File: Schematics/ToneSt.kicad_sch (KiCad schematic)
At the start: 18 parts

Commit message: Cosmetic upd
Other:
- moved on the sheet: Bass1, C51, C52, C53, C54, C55, C56, JP0, JP50, JP51, JP53, Middle1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

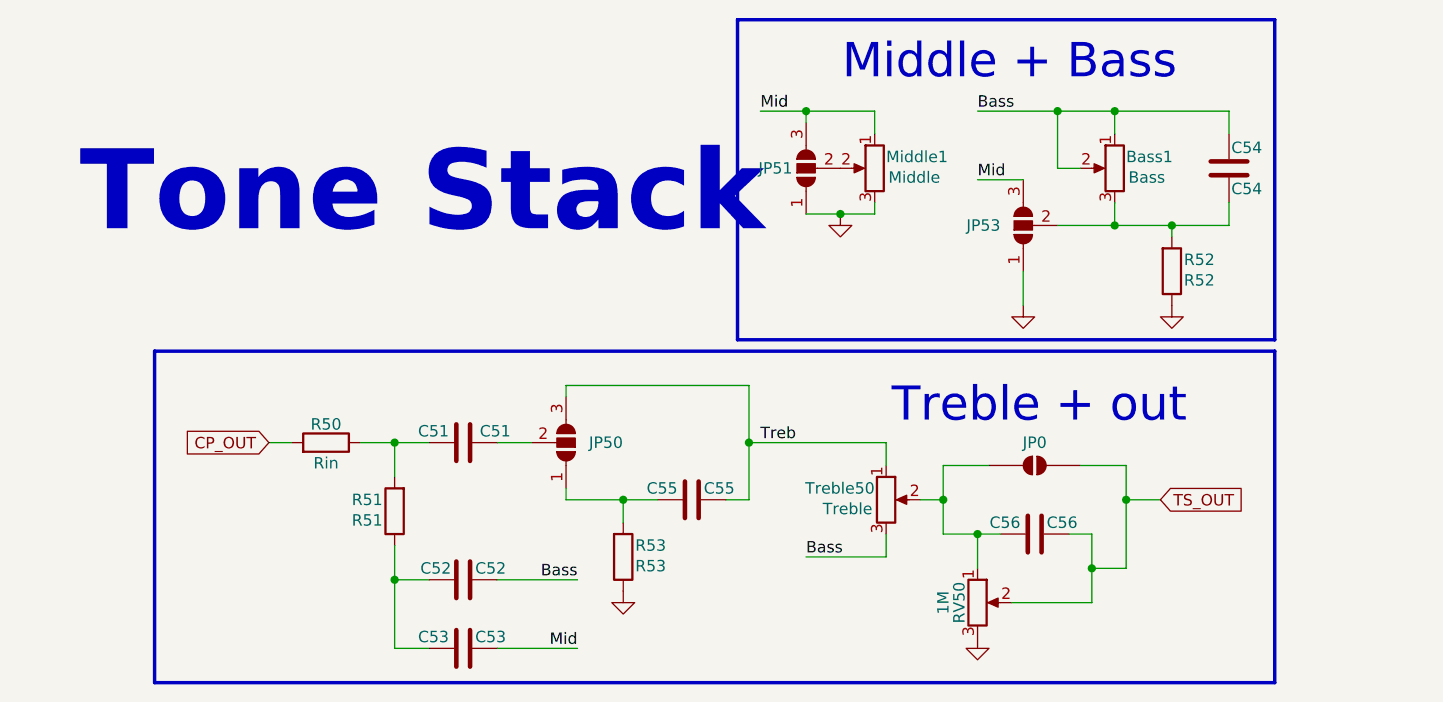
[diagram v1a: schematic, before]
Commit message: Schem. & Readme upd
volume control upd, optimized tone stack jumpers, small redactions in Readme
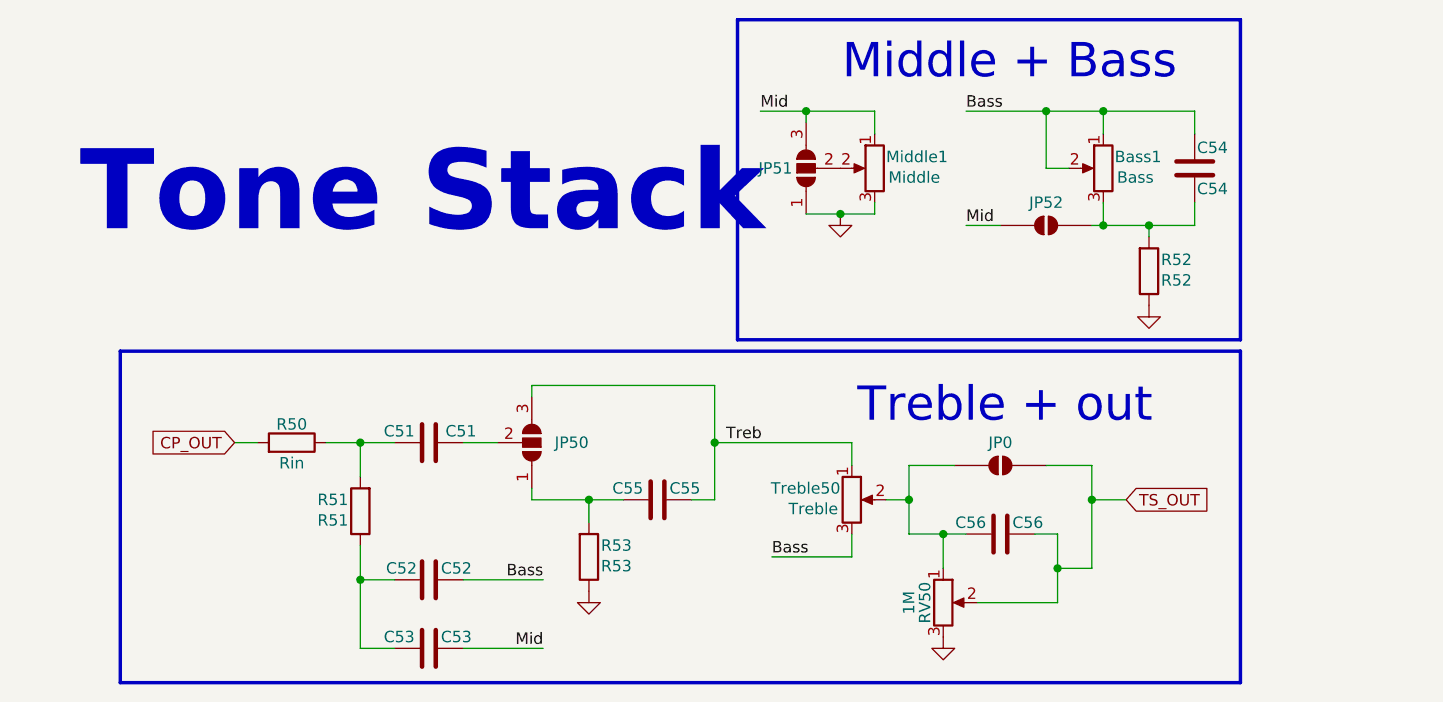
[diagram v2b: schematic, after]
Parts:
- removed JP53: SolderJumper_3_Open, Jumper:SolderJumper-3_P2.0mm_Open_TrianglePad1.0x1.5mm_NumberLabels, symbol Jumper:SolderJumper_3_Open
- added JP52: SolderJumper_2_Open, Jumper:SolderJumper-2_P1.3mm_Open_TrianglePad1.0x1.5mm, symbol Jumper:SolderJumper_2_Open
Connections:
- net Mid: now also JP52.1 (A)
- net at Bass1.3, C54.1, R52.2: now also JP52.2 (B)
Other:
- moved on the sheet: Bass1, C51, C52, C53, C54, C55, C56, JP0, JP50, R50, R51, R52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

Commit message: Version 0.1.0 Pre-Release
Reworked PCB, reanotated some components, changed some footprints
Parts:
- renumbered Treble50 to Treble1
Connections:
- net CP_OUT renamed BP_OUT
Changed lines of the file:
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@@
 		)
 	)
-	(global_label "CP_OUT"
+	(global_label "BP_OUT"
 		(shape input)
 		(at 26.67 60.96 180)
@@
 		)
 		(property "Intersheetrefs" "${INTERSHEET_REFS}"
-			(at 16.5486 60.96 0)
+			(at 16.799 60.96 0)
 			(hide yes)
 			(show_name no)
@@
 		(in_pos_files yes)
 		(dnp no)
-		(property "Reference" "Treble50"
+		(property "Reference" "Treble1"
 			(at 93.98 66.04 0)
 			(show_name no)
@@
 			(project "AMP-MA"
 				(path "/4094031b-a9da-4ac5-aaa1-42b342c92a3e/f803cc2a-45bd-4029-aa56-0c7cd35c7800"
-					(reference "Treble50")
+					(reference "Treble1")
 					(unit 1)
 				)

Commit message: Version 0.1.0 Release
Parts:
- renumbered JP0 to JP54
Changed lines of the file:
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@@
 		(in_pos_files yes)
 		(dnp no)
-		(property "Reference" "JP0"
+		(property "Reference" "JP54"
 			(at 111.76 60.96 0)
 			(show_name no)
@@
 			(project "AMP-MA"
 				(path "/4094031b-a9da-4ac5-aaa1-42b342c92a3e/f803cc2a-45bd-4029-aa56-0c7cd35c7800"
-					(reference "JP0")
+					(reference "JP54")
 					(unit 1)
 				)

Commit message: feat: start version 0.2.0 development
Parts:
- removed JP54: SolderJumper_2_Open, Jumper:SolderJumper-2_P1.3mm_Open_TrianglePad1.0x1.5mm, symbol Jumper:SolderJumper_2_Open
- added R54: 1R, Resistor_THT:R_Axial_DIN0207_L6.3mm_D2.5mm_P10.16mm_Horizontal, symbol Device:R
- C54, C55, C56, R52, R53, RV50: now not fitted
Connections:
- net GND: now also RV50.1; no longer RV50.3
- net TS_OUT: now also R54.1
- net at C56.1, Treble1.2: now also RV50.3, R54.2; no longer RV50.1
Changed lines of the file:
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@@
+	(wire
+		(pts
+			(xy 115.57 63.5) (xy 121.92 63.5)
+		)
+		(stroke
+			(width 0)
+			(type default)
+		)
+	)
 	(wire
 		(pts
@@
 	(wire
 		(pts
-			(xy 116.84 63.5) (xy 121.92 63.5)
-		)
-		(stroke
-			(width 0)
-			(type default)
-		)
-	)
-	(wire
-		(pts
 			(xy 123.19 36.83) (xy 133.35 36.83)
 		)
@@
 	(wire
 		(pts
-			(xy 101.6 63.5) (xy 106.68 63.5)
+			(xy 101.6 63.5) (xy 107.95 63.5)
 		)
 		(stroke
@@
 	)
 	(symbol
-		(lib_id "Jumper:SolderJumper_2_Open")
-		(at 111.76 63.5 0)
-		(unit 1)
-		(body_style 1)
-		(exclude_from_sim no)
-		(in_bom no)
-		(on_board yes)
-		(in_pos_files yes)
-		(dnp no)
-		(property "Reference" "JP54"
-			(at 111.76 60.96 0)
-			(show_name no)
-			(do_not_autoplace yes)
-			(effects
-				(font
-					(size 1.27 1.27)
-				)
-			)
-		)
-		(property "Value" "SolderJumper_2_Open"
-			(at 111.76 59.69 0)
-			(hide yes)
-			(show_name no)
-			(do_not_autoplace no)
-			(effects
-				(font
-					(size 1.27 1.27)
-				)
-			)
-		)
-		(property "Footprint" "Jumper:SolderJumper-2_P1.3mm_Open_TrianglePad1.0x1.5mm"
-			(at 111.76 63.5 0)
-			(hide yes)
-			(show_name no)
-			(do_not_autoplace no)
-			(effects
-				(font
-					(size 1.27 1.27)
-				)
-			)
-		)
-		(property "Datasheet" ""
-			(at 111.76 71.12 0)
-			(hide yes)
-			(show_name no)
-			(do_not_autoplace no)
-			(effects
-				(font
-					(size 1.27 1.27)
-				)
-			)
-		)
-		(property "Description" "Solder Jumper, 2-pole, open"
-			(at 111.76 68.58 0)
-			(hide yes)
-			(show_name no)
-			(do_not_autoplace no)
-			(effects
-				(font
-					(size 1.27 1.27)
-				)
-			)
-		)
-		(pin "2"
-		)
-		(pin "1"
-		)
-		(instances
-			(project "AMP-MA"
-				(path "/4094031b-a9da-4ac5-aaa1-42b342c92a3e/f803cc2a-45bd-4029-aa56-0c7cd35c7800"
-					(reference "JP54")
-					(unit 1)
-				)
-			)
-		)
-	)
-	(symbol
 		(lib_id "power:GND")
 		(at 93.98 35.56 0)
@@
 		(on_board yes)
 		(in_pos_files yes)
-		(dnp no)
+		(dnp yes)
 		(property "Reference" "C55"
 			(at 70.358 66.04 90)
@@
 		(on_board yes)
 		(in_pos_files yes)
-		(dnp no)
+		(dnp yes)
 		(property "Reference" "C54"
 			(at 133.604 28.194 0)
@@
 		(on_board yes)
 		(in_pos_files yes)
-		(dnp no)
+		(dnp yes)
 		(property "Reference" "R52"
 			(at 131.318 40.64 0)
@@
 		(on_board yes)
 		(in_pos_files yes)
-		(dnp no)
+		(dnp yes)
 		(property "Reference" "C56"
 			(at 108.458 69.85 90)
@@
 		(lib_id "Device:R_Potentiometer")
 		(at 105.41 78.74 0)
+		(mirror x)
 		(unit 1)
 		(body_style 1)
@@
 		(on_board yes)
 		(in_pos_files yes)
-		(dnp no)
+		(dnp yes)
 		(property "Reference" "RV50"
 			(at 103.378 78.74 90)
@@
 	)
 	(symbol
+		(lib_id "Device:R")
+		(at 111.76 63.5 270)
+		(mirror x)
+		(unit 1)
+		(body_style 1)
+		(exclude_from_sim no)
+		(in_bom yes)
+		(on_board yes)
+		(in_pos_files yes)
+		(dnp no)
+		(property "Reference" "R54"
+			(at 111.76 61.468 90)
+			(show_name no)
+			(do_not_autoplace no)
+			(effects
+				(font
+					(size 1.27 1.27)
+				)
+			)
+		)
+		(property "Value" "1R"
+			(at 111.76 65.786 90)
+			(show_name no)
+			(do_not_autoplace no)
+			(effects
+				(font
+					(size 1.27 1.27)
+				)
+			)
+		)
+		(property "Footprint" "Resistor_THT:R_Axial_DIN0207_L6.3mm_D2.5mm_P10.16mm_Horizontal"
+			(at 111.76 65.278 90)
+			(hide yes)
+			(show_name no)
+			(do_not_autoplace no)
+			(effects
+				(font
+					(size 1.27 1.27)
+				)
+			)
+		)
+		(property "Datasheet" ""
+			(at 111.76 63.5 0)
+			(hide yes)
+			(show_name no)
+			(do_not_autoplace no)
+			(effects
+				(font
+					(size 1.27 1.27)
+				)
+			)
+		)
+		(property "Description" "Resistor"
+			(at 111.76 63.5 0)
+			(hide yes)
+			(show_name no)
+			(do_not_autoplace no)
+			(effects
+				(font
+					(size 1.27 1.27)
+				)
+			)
+		)
+		(pin "2"
+		)
+		(pin "1"
+		)
+		(instances
+			(project "AMP-MA"
+				(path "/4094031b-a9da-4ac5-aaa1-42b342c92a3e/f803cc2a-45bd-4029-aa56-0c7cd35c7800"
+					(reference "R54")
+					(unit 1)
+				)
+			)
+		)
+	)
+	(symbol
 		(lib_id "power:GND")
 		(at 105.41 82.55 0)
@@
 		(on_board yes)
 		(in_pos_files yes)
-		(dnp no)
+		(dnp yes)
 		(property "Reference" "R53"
 			(at 69.088 72.39 0)
